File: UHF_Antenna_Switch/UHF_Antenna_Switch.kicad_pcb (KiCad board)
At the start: 2 copper layers, 0 parts

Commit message: Assign most footprints
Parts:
- added C1: 100p, Capacitor_SMD:C_0603_1608Metric_Pad1.08x0.95mm_HandSolder, F.Cu at (130.9, 75.5)
- added C10: 100n, Capacitor_SMD:C_0603_1608Metric_Pad1.08x0.95mm_HandSolder, F.Cu at (130.9, 80.5)
- added C11: 100p, Capacitor_SMD:C_0603_1608Metric_Pad1.08x0.95mm_HandSolder, F.Cu at (130.9, 83.0)
- added C2: 100p, Capacitor_SMD:C_0603_1608Metric_Pad1.08x0.95mm_HandSolder, F.Cu at (130.9, 78.0)
- added D2: 1N4148W, Diode_SMD:D_SOD-123, F.Cu at (158.1, 51.7)
- added D3: 1N4148W, Diode_SMD:D_SOD-123, F.Cu at (158.1, 70.2)
- added D4: LED, LED_SMD:LED_0603_1608Metric_Pad1.05x0.95mm_HandSolder, F.Cu at (138.3, 51.3)
- added D5: LED, LED_SMD:LED_0603_1608Metric_Pad1.05x0.95mm_HandSolder, F.Cu at (138.3, 53.9)
- added D6: LED, LED_SMD:LED_0603_1608Metric_Pad1.05x0.95mm_HandSolder, F.Cu at (138.3, 56.5)
- added D7: LED, LED_SMD:LED_0603_1608Metric_Pad1.05x0.95mm_HandSolder, F.Cu at (138.3, 59.1)
- added D8: LED, LED_SMD:LED_0603_1608Metric_Pad1.05x0.95mm_HandSolder, F.Cu at (138.3, 61.7)
- added D9: LED, LED_SMD:LED_0603_1608Metric_Pad1.05x0.95mm_HandSolder, F.Cu at (138.3, 64.2)
- added J1: Conn_SMA_Female, Connector_Coaxial:SMA_Amphenol_901-143_Horizontal, F.Cu at (111.8, 62.5)
- added J2: Conn_SMA_Female, Connector_Coaxial:SMA_Amphenol_901-143_Horizontal, F.Cu at (121.5, 62.5)
- added J3: Conn_SMA_Female, Connector_Coaxial:SMA_Amphenol_901-143_Horizontal, F.Cu at (131.2, 62.5)
- added K3: HF3-51, Relay_SMD:Relay_SPDT_AXICOM_HF3Series_50ohms_Pitch1.27mm, F.Cu at (149.4, 58.3)
- added K4: HF3-51, Relay_SMD:Relay_SPDT_AXICOM_HF3Series_50ohms_Pitch1.27mm, F.Cu at (149.4, 76.9)
- added Q2: 2N7002, Package_TO_SOT_SMD:SOT-23, F.Cu at (157.6, 60.6)
- added Q3: 2N7002, Package_TO_SOT_SMD:SOT-23, F.Cu at (157.6, 79.1)
- added R10: 5k1, Resistor_SMD:R_0603_1608Metric_Pad0.98x0.95mm_HandSolder, F.Cu at (135.2, 80.5)
- added R11: 5k1, Resistor_SMD:R_0603_1608Metric_Pad0.98x0.95mm_HandSolder, F.Cu at (135.2, 83.0)
- added R12: 5k1, Resistor_SMD:R_0603_1608Metric_Pad0.98x0.95mm_HandSolder, F.Cu at (135.2, 85.5)
- added R2: 50, Resistor_SMD:R_0603_1608Metric_Pad0.98x0.95mm_HandSolder, F.Cu at (130.9, 85.5)
- added R3: 100, Resistor_SMD:R_0603_1608Metric_Pad0.98x0.95mm_HandSolder, F.Cu at (157.4, 54.6)
- added R4: 10k, Resistor_SMD:R_0603_1608Metric_Pad0.98x0.95mm_HandSolder, F.Cu at (157.4, 57.1)
- added R5: 100, Resistor_SMD:R_0603_1608Metric_Pad0.98x0.95mm_HandSolder, F.Cu at (157.4, 73.2)
- added R6: 10k, Resistor_SMD:R_0603_1608Metric_Pad0.98x0.95mm_HandSolder, F.Cu at (157.4, 75.7)
- added R7: 5k1, Resistor_SMD:R_0603_1608Metric_Pad0.98x0.95mm_HandSolder, F.Cu at (130.9, 88.1)
- added R8: 5k1, Resistor_SMD:R_0603_1608Metric_Pad0.98x0.95mm_HandSolder, F.Cu at (135.2, 75.5)
- added R9: 5k1, Resistor_SMD:R_0603_1608Metric_Pad0.98x0.95mm_HandSolder, F.Cu at (135.2, 78.0)
- added SW1: SW_SP3T, Button_Switch_SMD:SW_SP3T_PCM13, F.Cu at (135.1, 70.3)
- added U1: LTC5507ES6, Package_TO_SOT_SMD:TSOT-23-6_HandSoldering, F.Cu at (132.2, 91.7)
- added U2: PAT1220-C-10DB, RF_Converter:RF_Attenuator_Susumu_PAT1220, F.Cu at (137.9, 91.2)
- added U4: RP2040-Zero, 00-project-footprints:RP2040 Zero, F.Cu at (107.8, 94.4)
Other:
- board outline added: 10.7 x 19.8 mm

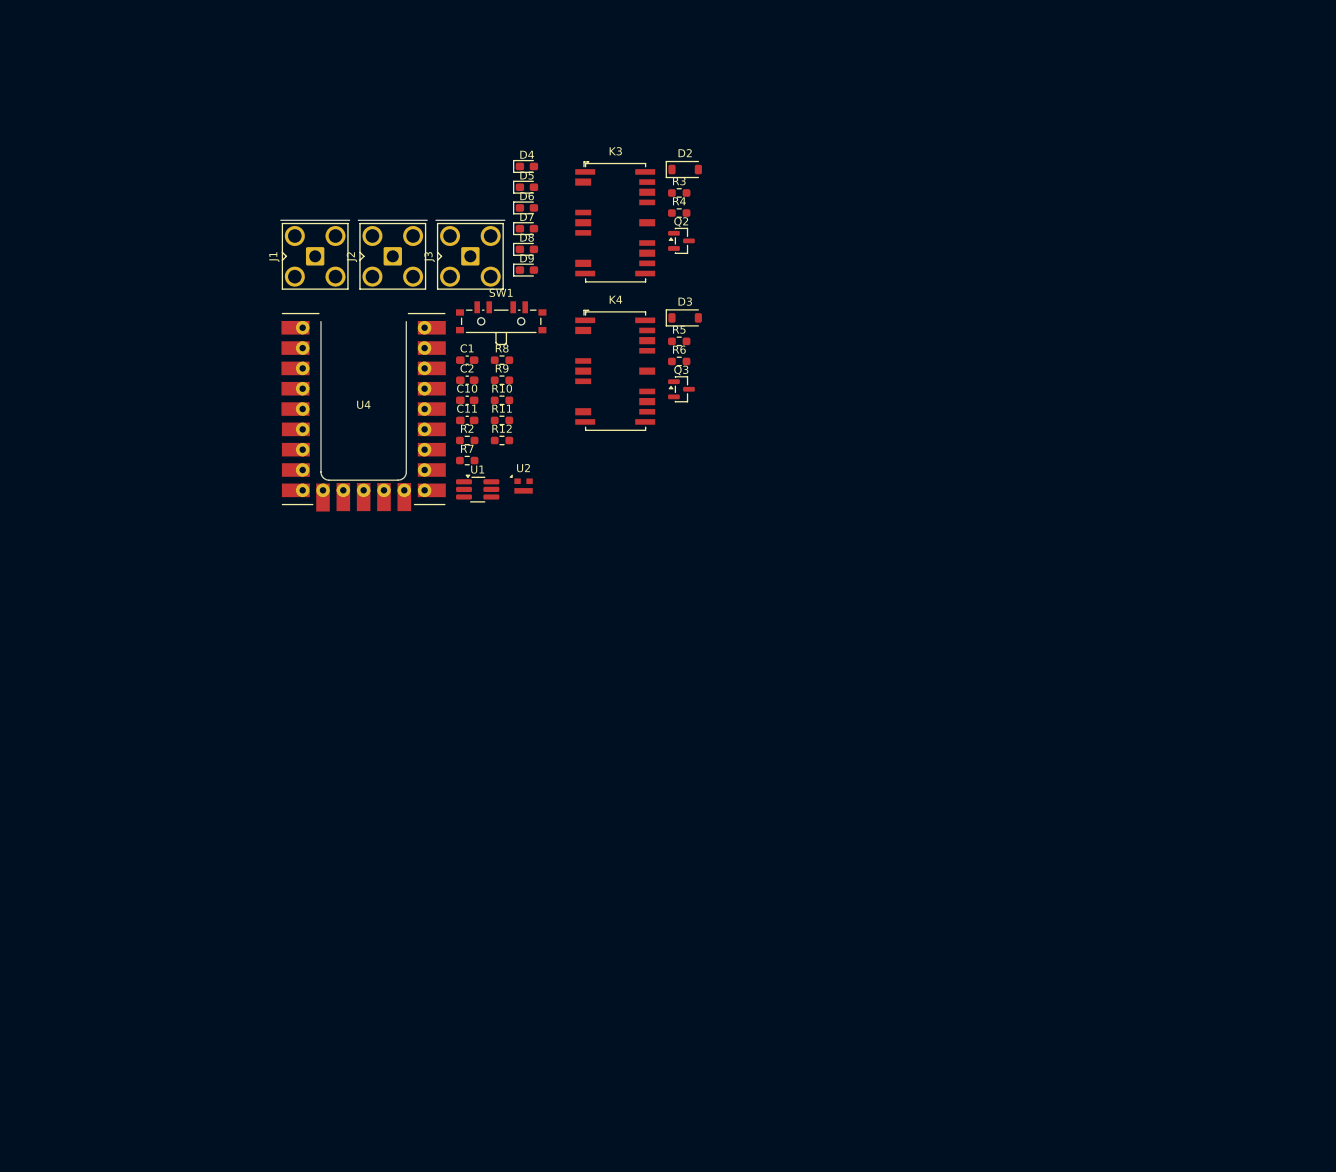
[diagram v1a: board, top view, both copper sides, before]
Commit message: Add N-Type PCB connector footprint
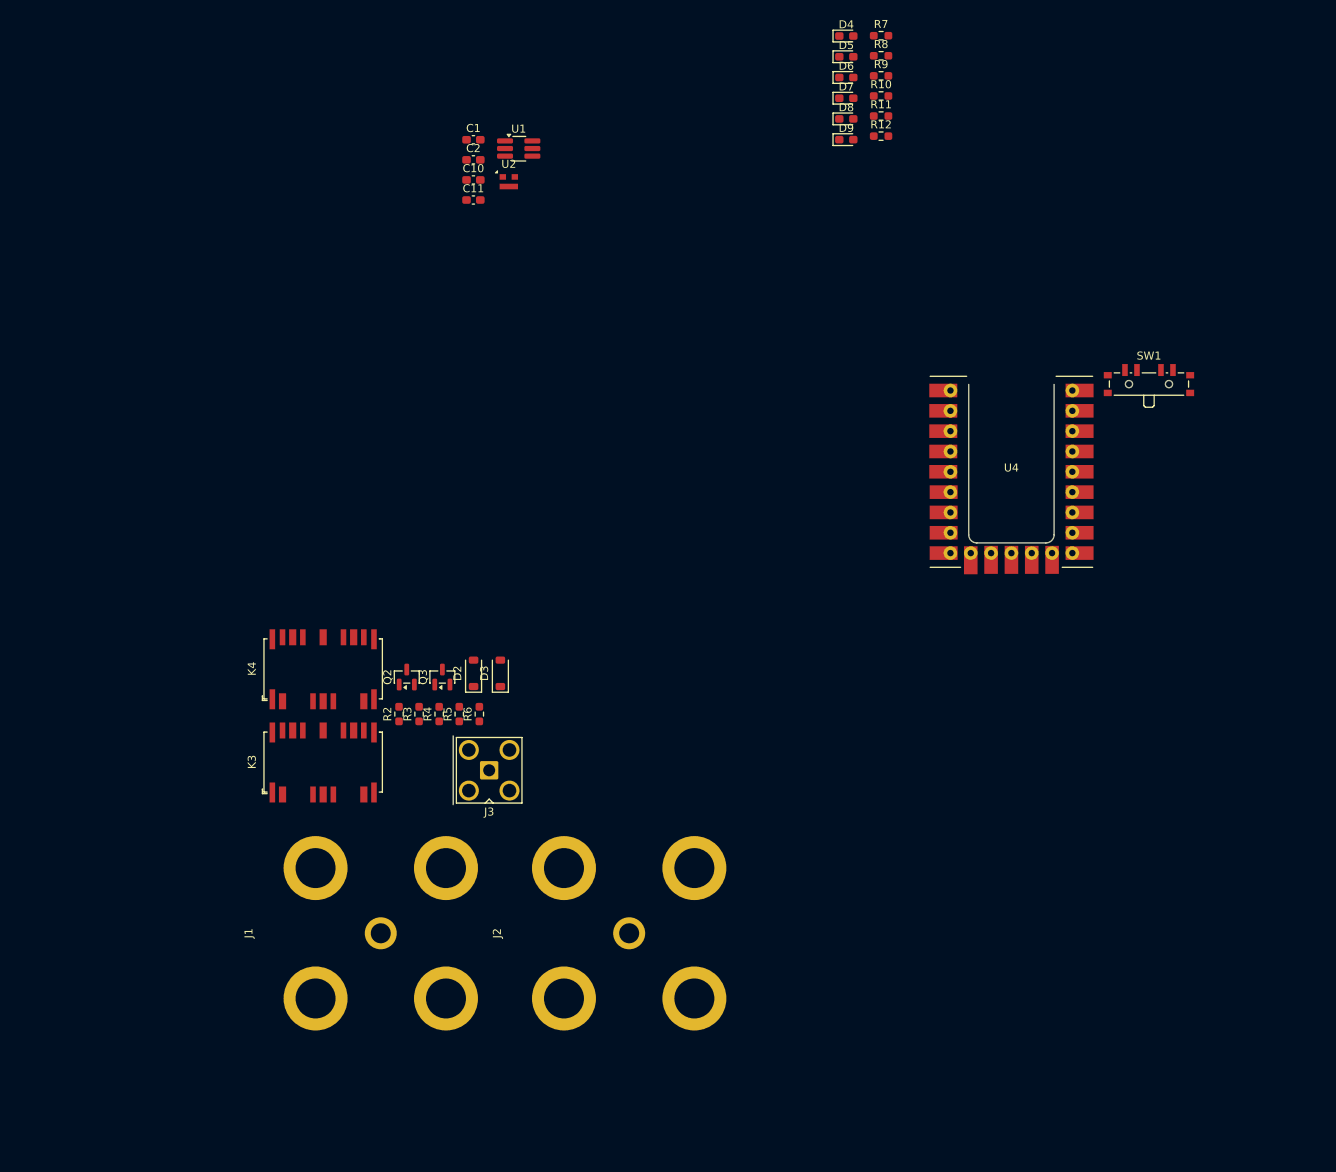
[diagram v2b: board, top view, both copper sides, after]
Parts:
- J1: value Conn_SMA_Female -> Conn_N_Type_Female; footprint Connector_Coaxial:SMA_Amphenol_901-143_Horizontal -> 00-project-footprints:Amphenol N Jack 172234
- J2: value Conn_SMA_Female -> Conn_SO-239; footprint Connector_Coaxial:SMA_Amphenol_901-143_Horizontal -> 00-project-footprints:Amphenol N Jack 172234
- moved J2 89.6 mm to (151.1, 147.1), turned to 90 degrees
- moved J1 85.0 mm to (120.0, 147.1), turned to 90 degrees
- moved SW1 81.3 mm to (216.1, 78.2)
- moved U4 81.3 mm to (188.7, 102.3)
- moved K3 76.7 mm to (112.8, 125.8), turned to 90 degrees
- moved R7 74.1 mm to (182.6, 35.0)
- moved R3 72.8 mm to (124.8, 119.7), turned to 90 degrees
- moved R4 69.4 mm to (127.3, 119.7), turned to 90 degrees
- moved D2 68.3 mm to (131.7, 114.7), turned to 90 degrees
- moved Q2 64.4 mm to (123.3, 115.1), turned to 90 degrees
- moved J3 64.3 mm to (133.6, 126.8), turned to 90 degrees
- moved R10 60.8 mm to (182.6, 42.5)
- moved R11 60.8 mm to (182.6, 45.0)
- moved R12 60.8 mm to (182.6, 47.5)
- moved R8 60.8 mm to (182.6, 37.5)
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
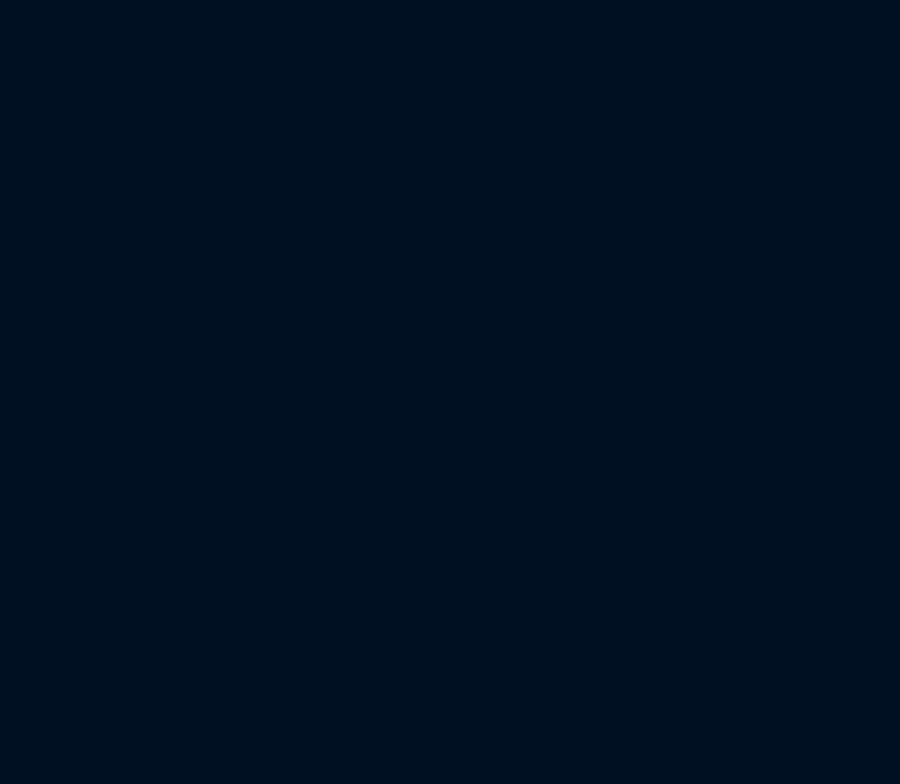
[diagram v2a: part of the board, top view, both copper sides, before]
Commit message: Add 3V3 power connector
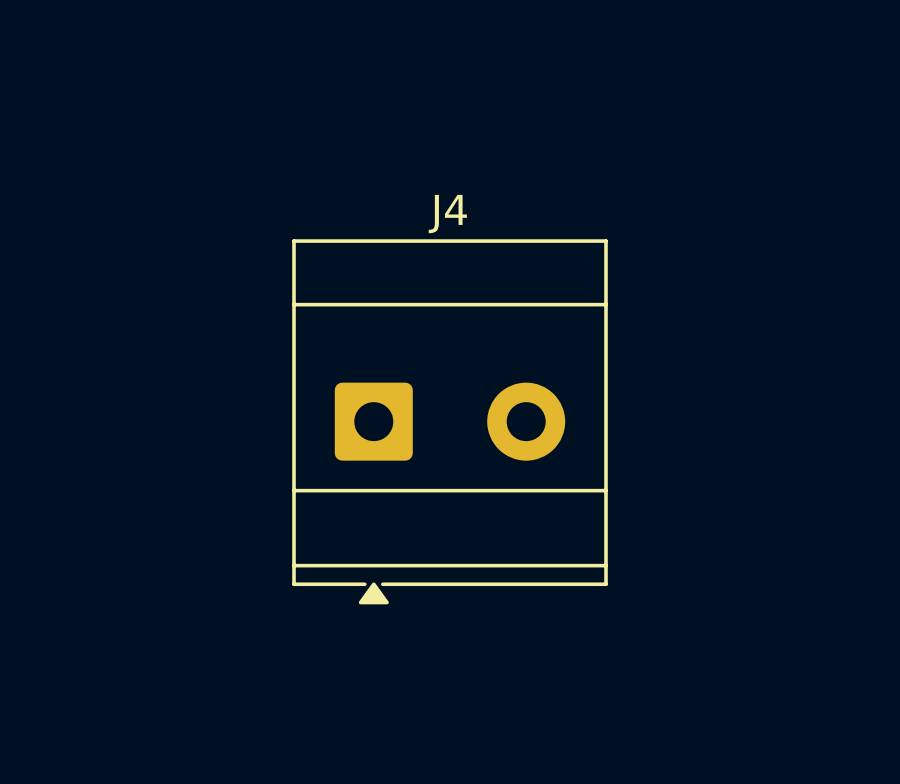
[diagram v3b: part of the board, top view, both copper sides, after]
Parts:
- added J4: Screw_Terminal_01x02, TerminalBlock_Phoenix:TerminalBlock_Phoenix_MKDS-3-2-5.08_1x02_P5.08mm_Horizontal, F.Cu at (162.6, 83.4)

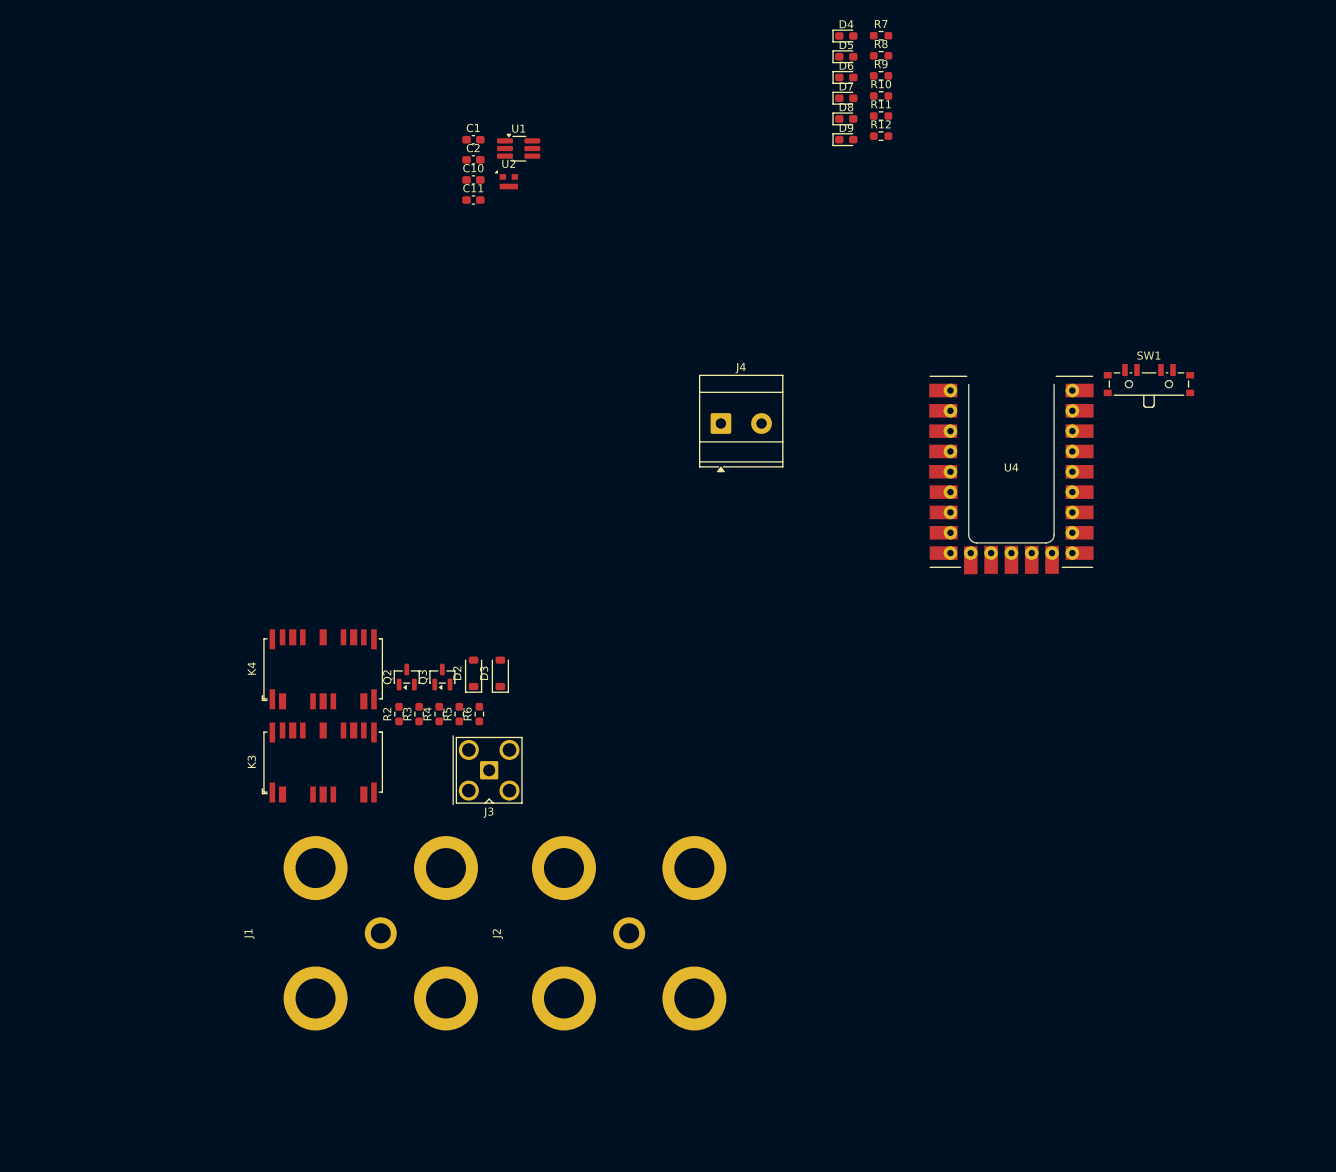
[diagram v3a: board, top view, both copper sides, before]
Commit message: Add preliminary footprint to directional coupler and begin layout
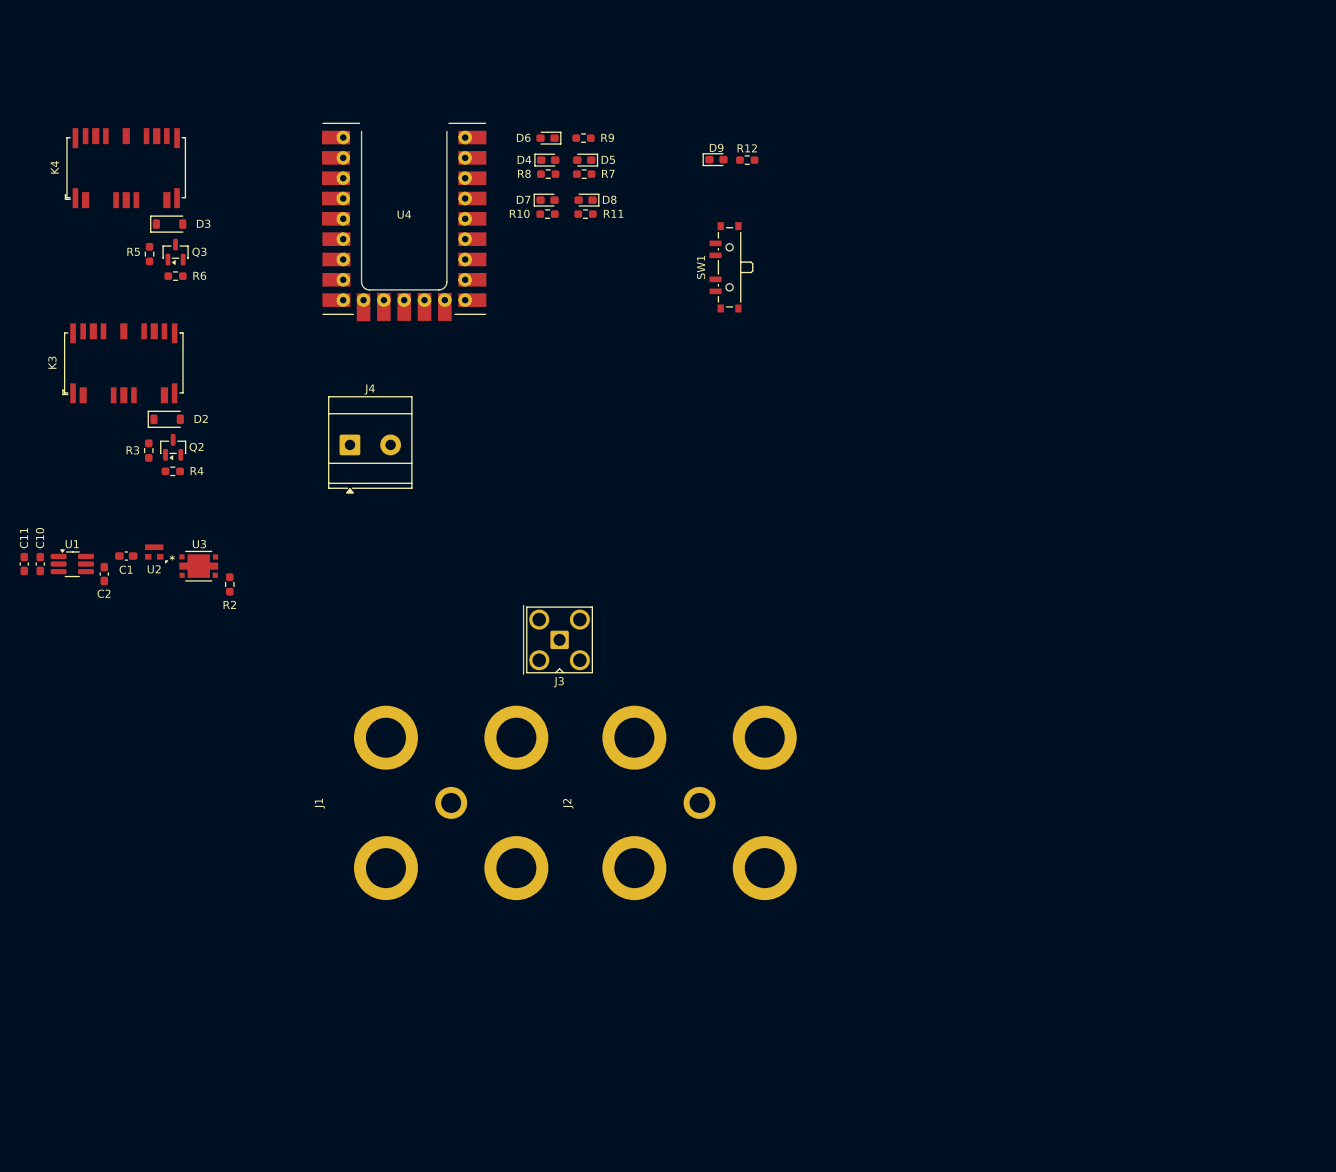
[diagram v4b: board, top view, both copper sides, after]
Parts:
- added U3: X4C09F1-30S, 00-project-footprints:X4C09F1 - 30S, F.Cu at (97.4, 98.9)
- moved U4 82.2 mm to (112.8, 70.7)
- moved U1 76.2 mm to (81.5, 101.0)
- moved C10 72.4 mm to (77.5, 101.0), turned to -90 degrees
- moved C11 72.3 mm to (75.5, 101.0), turned to -90 degrees
- moved D3 69.7 mm to (93.7, 58.5), turned to 0 degrees
- moved C2 69.4 mm to (85.5, 102.2), turned to 90 degrees
- moved R5 69.3 mm to (91.2, 62.2), turned to -90 degrees
- moved C1 67.8 mm to (88.2, 100.0), turned to 180 degrees
- moved K4 67.3 mm to (88.2, 51.5)
- moved R6 66.6 mm to (94.4, 65.0), turned to 0 degrees
- moved U2 64.1 mm to (91.7, 99.5), turned to 180 degrees
- moved Q3 62.7 mm to (94.4, 62.0)
- moved K3 55.8 mm to (87.9, 75.9)
- moved SW1 54.6 mm to (163.3, 63.9), turned to 90 degrees
- moved D2 49.7 mm to (93.3, 82.9), turned to 0 degrees
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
